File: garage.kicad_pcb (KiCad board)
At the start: 2 copper layers, 9 parts, among them P1 CONN_02X25, P2 CONN_01X02, P3 CONN_02X25, P4 CONN_01X20, P5 CONN_01X20, Q1 ZTX1049a

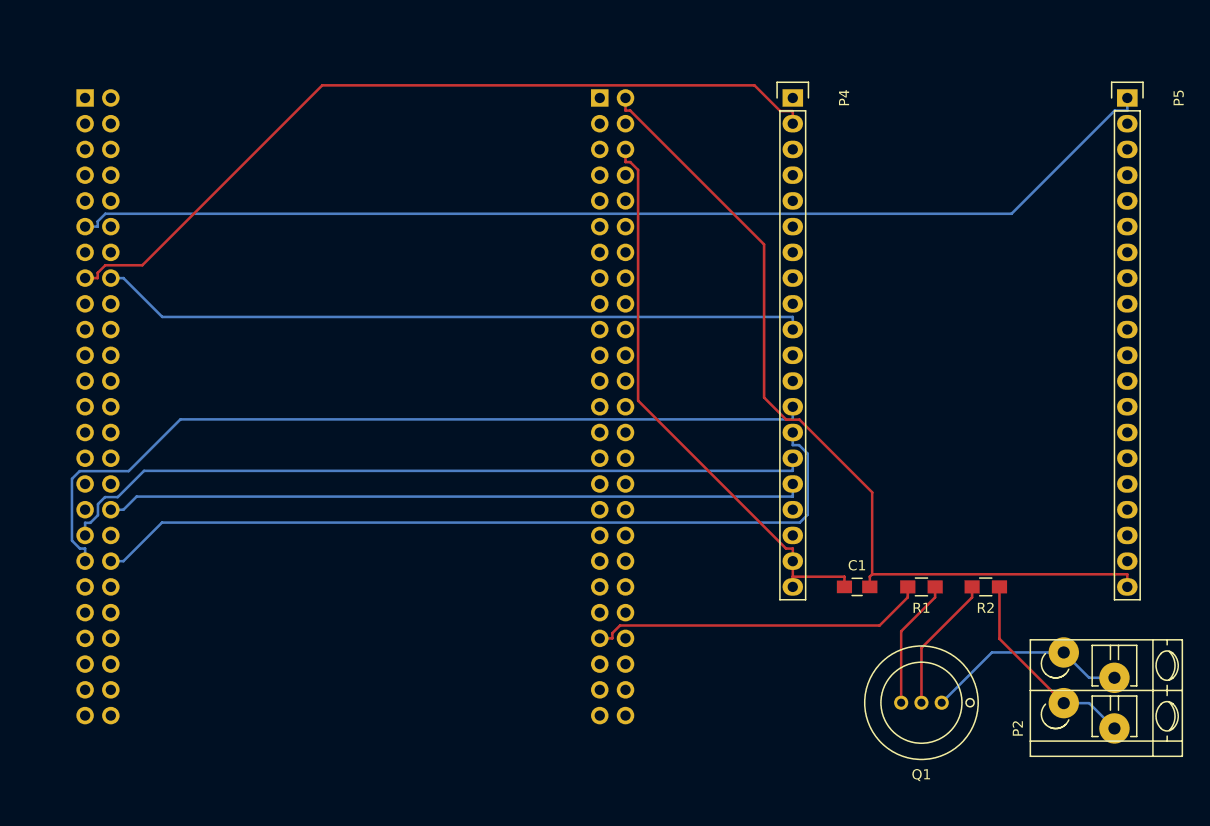
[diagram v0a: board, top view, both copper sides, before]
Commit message: Added board outline
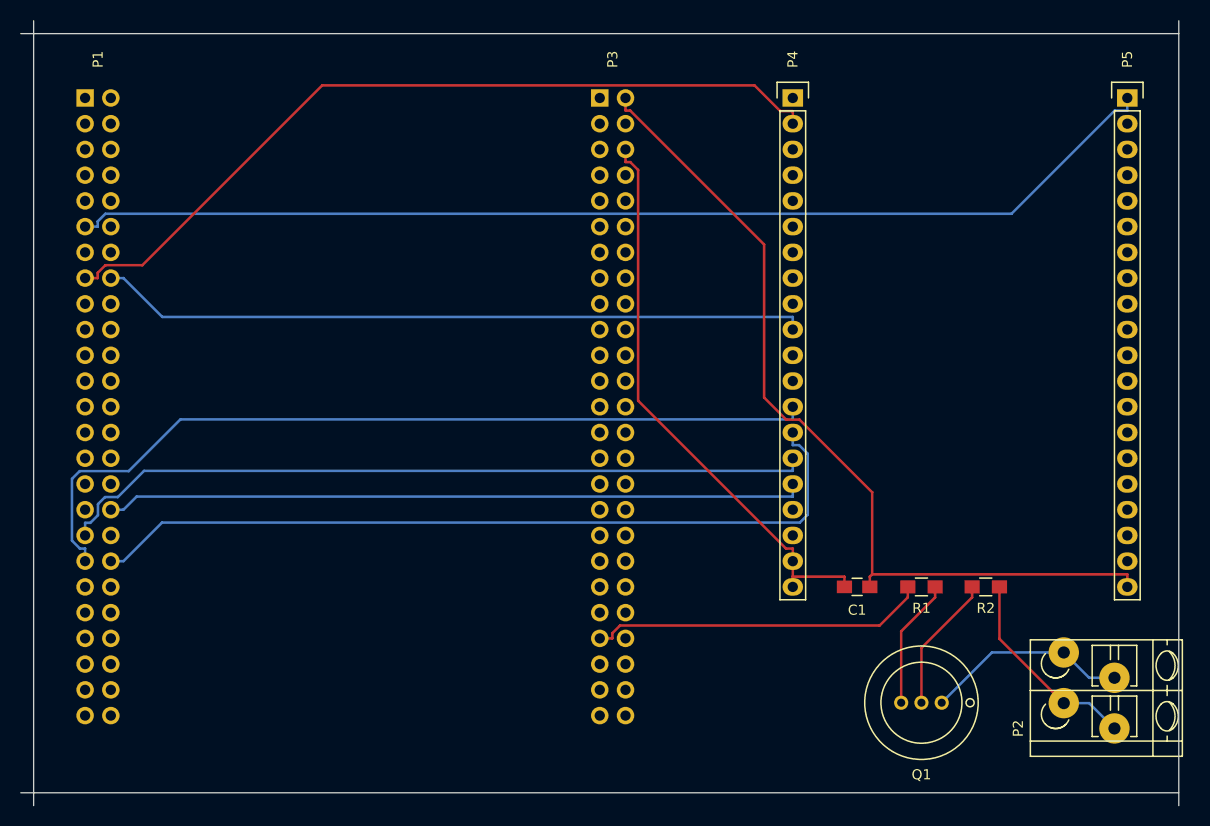
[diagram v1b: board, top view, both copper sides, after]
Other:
- board outline added: 114.3 x 77.5 mm

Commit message: Reduced size of PCB by half
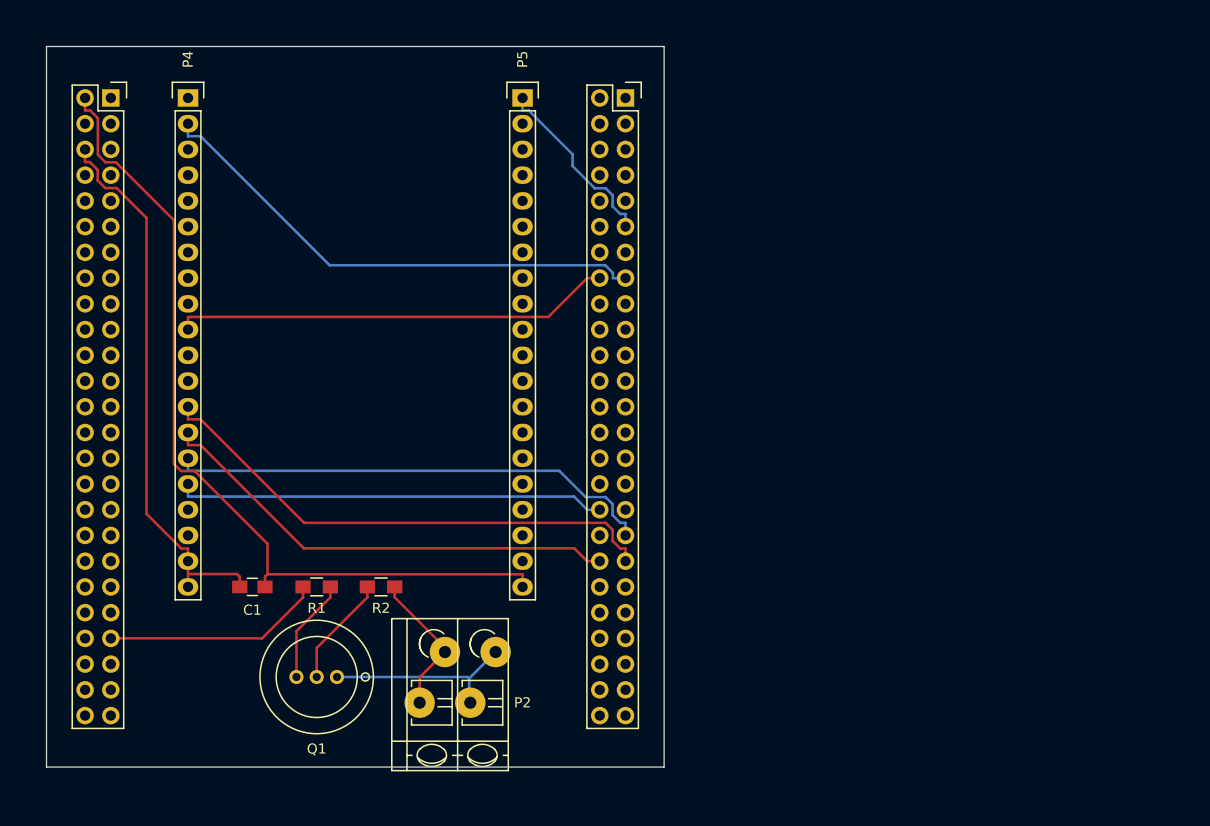
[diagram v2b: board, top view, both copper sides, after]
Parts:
- P1, P3: moved to F.Cu
- moved P2 68.6 mm to (91.4, 96.5), turned to 0 degrees
- moved Q1 59.7 mm to (81.3, 94.0)
- moved P4 59.7 mm to (68.6, 36.8)
- moved C1 59.7 mm to (74.9, 85.1)
- moved P5 59.7 mm to (101.6, 36.8)
- moved R1 59.7 mm to (81.3, 85.1)
- moved R2 59.7 mm to (87.6, 85.1)
- moved P1 53.3 mm to (111.8, 36.8)
- moved P3 48.3 mm to (61.0, 36.8)
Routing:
- net PA1: track 109.2 -> 18.2 mm
- net CTS: track 79.8 -> 46.6 mm
- net RTS: track 83.8 -> 51.6 mm
- net GPIO2: track 80.3 -> 50.5 mm
- net TX: track 75.1 -> 48.4 mm
- net GPIO9: track 70.1 -> 43.5 mm
- net RX: track 69.1 -> 42.4 mm
- net PA8: track 33.4 -> 21.7 mm
- net Garage+: track 20.1 -> 14.5 mm
- net Net-(Q1-Pad3): track 12.8 -> 10.3 mm
- net Net-(Q1-Pad2): track 13.5 -> 11.0 mm
- net GND: track 85.9 -> 83.9 mm
- net 3V: track 56.8 -> 54.9 mm
- net Garage-: track 20.1 -> 19.2 mm
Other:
- board size 114.3 x 77.5 mm -> 61 x 71.1 mm
- rule via_min_drill: 0.508 -> 0.3302
- rule via_min_size: 0.889 -> 0.6858

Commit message: Added ground plane
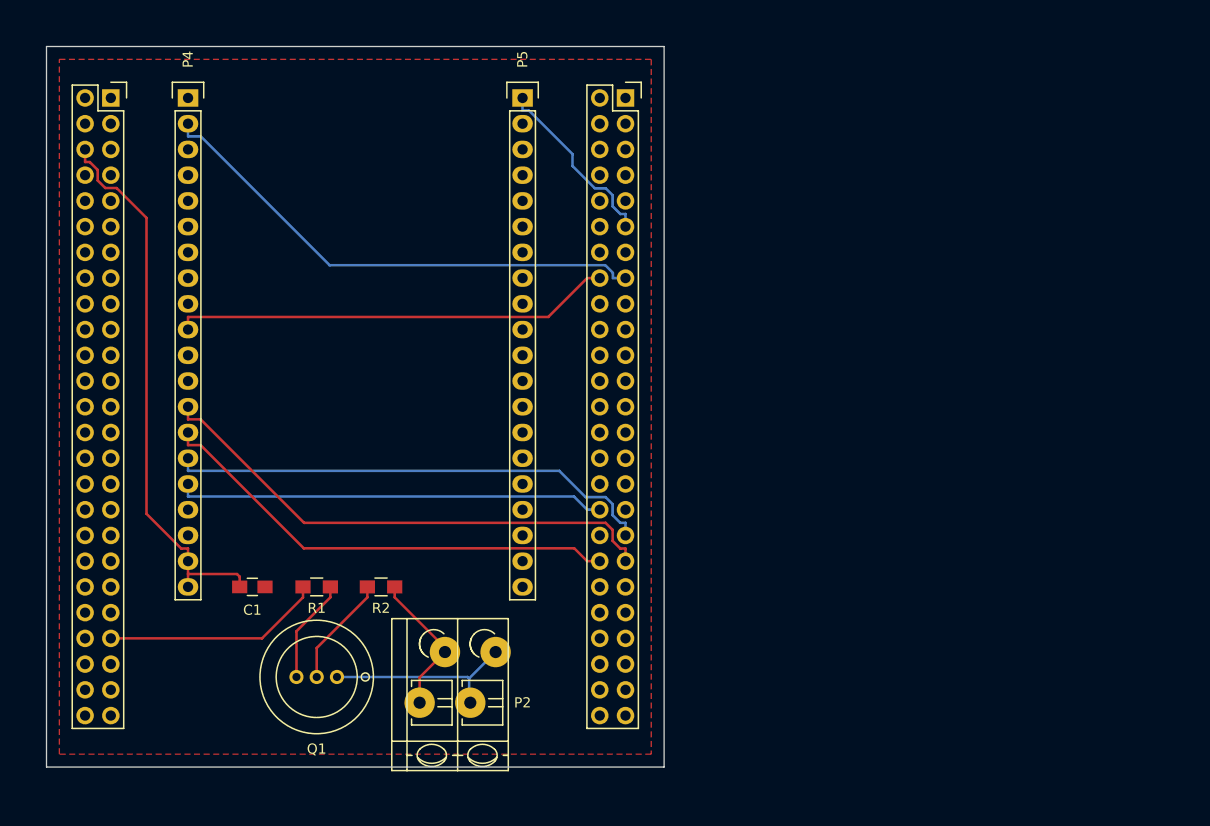
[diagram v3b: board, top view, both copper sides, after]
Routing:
- net GND: track 83.9 -> 0.00 mm
- added copper zone on F.Cu, net GND
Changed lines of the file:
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@@
     (thickness 1.6)
     (drawings 4)
-    (tracks 101)
+    (tracks 85)
     (zones 0)
     (modules 9)
@@
   (segment (start 68.58 83.82) (end 73.4163 83.82) (width 0.254) (layer F.Cu) (net 1))
   (segment (start 73.68 85.09) (end 73.68 84.0837) (width 0.254) (layer F.Cu) (net 1))
-  (segment (start 101.6 85.09) (end 101.6 83.8451) (width 0.254) (layer F.Cu) (net 2))
-  (segment (start 76.18 85.09) (end 76.18 84.0837) (width 0.254) (layer F.Cu) (net 2))
-  (segment (start 58.42 36.83) (end 58.42 38.0749) (width 0.254) (layer F.Cu) (net 2))
-  (segment (start 58.9358 38.0749) (end 58.42 38.0749) (width 0.254) (layer F.Cu) (net 2))
-  (segment (start 59.69 38.8291) (end 58.9358 38.0749) (width 0.254) (layer F.Cu) (net 2))
-  (segment (start 59.69 42.4461) (end 59.69 38.8291) (width 0.254) (layer F.Cu) (net 2))
-  (segment (start 60.4239 43.18) (end 59.69 42.4461) (width 0.254) (layer F.Cu) (net 2))
-  (segment (start 61.4707 43.18) (end 60.4239 43.18) (width 0.254) (layer F.Cu) (net 2))
-  (segment (start 67.1826 48.8919) (end 61.4707 43.18) (width 0.254) (layer F.Cu) (net 2))
-  (segment (start 67.1826 72.9459) (end 67.1826 48.8919) (width 0.254) (layer F.Cu) (net 2))
-  (segment (start 67.8967 73.66) (end 67.1826 72.9459) (width 0.254) (layer F.Cu) (net 2))
-  (segment (start 69.2515 73.66) (end 67.8967 73.66) (width 0.254) (layer F.Cu) (net 2))
-  (segment (start 76.4186 80.8271) (end 69.2515 73.66) (width 0.254) (layer F.Cu) (net 2))
-  (segment (start 76.4186 83.8451) (end 76.4186 80.8271) (width 0.254) (layer F.Cu) (net 2))
-  (segment (start 101.6 83.8451) (end 76.4186 83.8451) (width 0.254) (layer F.Cu) (net 2))
-  (segment (start 76.4186 83.8451) (end 76.18 84.0837) (width 0.254) (layer F.Cu) (net 2))
   (segment (start 111.2442 48.2851) (end 111.76 48.2851) (width 0.254) (layer B.Cu) (net 13))
   (segment (start 110.49 47.5309) (end 111.2442 48.2851) (width 0.254) (layer B.Cu) (net 13))
@@
   (segment (start 82.63 86.1213) (end 79.28 89.4713) (width 0.254) (layer F.Cu) (net 134))
   (segment (start 82.63 85.09) (end 82.63 86.1213) (width 0.254) (layer F.Cu) (net 134))
+  (zone (net 2) (net_name GND) (layer F.Cu) (hatch edge 0.508)
+    (connect_pads (clearance 0.508))
+    (min_thickness 0.254)
+    (fill yes (arc_segments 16) (thermal_gap 0.508) (thermal_bridge_width 0.508))
+    (polygon
+      (pts
+        (xy 114.3 101.6) (xy 55.88 101.6) (xy 55.88 33.02) (xy 114.3 33.02)
+      )
+    )
+  )
 )

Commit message: Updated power and ground planes
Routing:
- net 3V: track 54.9 -> 0.00 mm
- net GND: track 0.00 -> 4.34 mm, vias 0 -> 1
- added copper zone on F.Cu, net 3V
- added copper zone on B.Cu, net GND
- removed copper zone on F.Cu, net GND
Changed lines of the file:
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@@
     (thickness 1.6)
     (drawings 4)
-    (tracks 85)
+    (tracks 72)
     (zones 0)
     (modules 9)
@@
   (gr_line (start 115.57 31.75) (end 115.57 102.87) (angle 90) (layer Edge.Cuts) (width 0.1))
   (gr_line (start 54.61 31.75) (end 115.57 31.75) (angle 90) (layer Edge.Cuts) (width 0.1))
-  (segment (start 58.42 41.91) (end 58.42 43.1549) (width 0.254) (layer F.Cu) (net 1))
-  (segment (start 68.58 82.55) (end 68.58 81.3051) (width 0.254) (layer F.Cu) (net 1))
-  (segment (start 67.9117 81.3051) (end 68.58 81.3051) (width 0.254) (layer F.Cu) (net 1))
-  (segment (start 64.4833 77.8767) (end 67.9117 81.3051) (width 0.254) (layer F.Cu) (net 1))
-  (segment (start 64.4833 48.672) (end 64.4833 77.8767) (width 0.254) (layer F.Cu) (net 1))
-  (segment (start 61.5313 45.72) (end 64.4833 48.672) (width 0.254) (layer F.Cu) (net 1))
-  (segment (start 60.4086 45.72) (end 61.5313 45.72) (width 0.254) (layer F.Cu) (net 1))
-  (segment (start 59.6649 44.9763) (end 60.4086 45.72) (width 0.254) (layer F.Cu) (net 1))
-  (segment (start 59.6649 43.9329) (end 59.6649 44.9763) (width 0.254) (layer F.Cu) (net 1))
-  (segment (start 58.8869 43.1549) (end 59.6649 43.9329) (width 0.254) (layer F.Cu) (net 1))
-  (segment (start 58.42 43.1549) (end 58.8869 43.1549) (width 0.254) (layer F.Cu) (net 1))
-  (segment (start 68.58 85.09) (end 68.58 83.82) (width 0.254) (layer F.Cu) (net 1))
-  (segment (start 68.58 83.82) (end 68.58 82.55) (width 0.254) (layer F.Cu) (net 1))
-  (segment (start 73.4163 83.82) (end 73.68 84.0837) (width 0.254) (layer F.Cu) (net 1))
-  (segment (start 68.58 83.82) (end 73.4163 83.82) (width 0.254) (layer F.Cu) (net 1))
-  (segment (start 73.68 85.09) (end 73.68 84.0837) (width 0.254) (layer F.Cu) (net 1))
+  (segment (start 76.18 85.09) (end 76.18 82.57) (width 0.254) (layer F.Cu) (net 2))
+  (via (at 77.47 81.28) (size 0.889) (layers F.Cu B.Cu) (net 2))
+  (segment (start 76.18 82.57) (end 77.47 81.28) (width 0.254) (layer F.Cu) (net 2))
   (segment (start 111.2442 48.2851) (end 111.76 48.2851) (width 0.254) (layer B.Cu) (net 13))
   (segment (start 110.49 47.5309) (end 111.2442 48.2851) (width 0.254) (layer B.Cu) (net 13))
@@
   (segment (start 82.63 86.1213) (end 79.28 89.4713) (width 0.254) (layer F.Cu) (net 134))
   (segment (start 82.63 85.09) (end 82.63 86.1213) (width 0.254) (layer F.Cu) (net 134))
-  (zone (net 2) (net_name GND) (layer F.Cu) (hatch edge 0.508)
+  (zone (net 1) (net_name 3V) (layer F.Cu) (hatch edge 0.508)
     (connect_pads (clearance 0.508))
     (min_thickness 0.254)
+    (fill yes (arc_segments 16) (thermal_gap 0.508) (thermal_bridge_width 0.508))
+    (polygon
+      (pts
+        (xy 114.3 101.6) (xy 55.88 101.6) (xy 55.88 33.02) (xy 114.3 33.02)
+      )
+    )
+  )
+  (zone (net 2) (net_name GND) (layer B.Cu) (hatch edge 0.508)
+    (connect_pads (clearance 0.508))
+    (min_thickness 0.254)

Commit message: Added silkscreen
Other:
- board text added: "BlueTooth Garage Opener"
- board text added: "Rev A"
- board text added: "SESAME"
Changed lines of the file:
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@@
     (area 56.380999 31.841 120.022334 103.899)
     (thickness 1.6)
-    (drawings 4)
+    (drawings 7)
     (tracks 72)
     (zones 0)
@@
   (page A4)
   (layers
-    (0 F.Cu signal)
-    (31 B.Cu signal)
+    (0 F.Cu signal hide)
+    (31 B.Cu signal hide)
     (32 B.Adhes user)
     (33 F.Adhes user)
@@
     )
   )
+  (gr_text "Rev A" (at 110.49 100.33) (layer B.SilkS)
+    (effects (font (size 0.8 0.8) (thickness 0.12)) (justify mirror))
+  )
+  (gr_text "BlueTooth Garage Opener" (at 69.215 98.425) (layer F.SilkS)
+    (effects (font (size 0.8 0.6) (thickness 0.15) italic))
+  )
+  (gr_text SESAME (at 69.215 96.52) (layer F.SilkS)
+    (effects (font (size 1.5 1.5) (thickness 0.3)))
+  )
   (gr_line (start 54.61 102.87) (end 54.61 31.75) (angle 90) (layer Edge.Cuts) (width 0.1))

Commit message: updated labels
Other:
- rule via_min_size: 0.6858 -> 0.889
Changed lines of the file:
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@@
   (page A4)
   (layers
-    (0 F.Cu signal hide)
-    (31 B.Cu signal hide)
+    (0 F.Cu signal)
+    (31 B.Cu signal)
     (32 B.Adhes user)
     (33 F.Adhes user)
@@
     (via_size 0.889)
     (via_drill 0.635)
-    (via_min_size 0.6858)
+    (via_min_size 0.889)
     (via_min_drill 0.3302)
     (uvia_size 0.508)
@@
     (visible_elements 7FFFFFFF)
     (pcbplotparams
-      (layerselection 0x00030_80000001)
-      (usegerberextensions false)
+      (layerselection 0x010f0_80000001)
+      (usegerberextensions true)
       (excludeedgelayer true)
       (linewidth 0.100000)
@@
       (outputformat 1)
       (mirror false)
-      (drillshape 1)
+      (drillshape 0)
       (scaleselection 1)
-      (outputdirectory ""))
+      (outputdirectory gerber/))
   )
   (net 0 "")

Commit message: Changed traces to match schematic update.
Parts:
- Q1: value ZTX1049a -> 2N3904
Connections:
- P2 pad 2: Garage- -> GND
- Q1 pad 1: Garage- -> GND
- R1 pad 1: Net-(Q1-Pad3) -> Net-(Q1-Pad2)
- R2 pad 2: Net-(Q1-Pad2) -> Net-(Q1-Pad3)
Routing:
- net Garage-: track 19.2 -> 0.00 mm
- net GND: track 4.34 -> 23.6 mm
- net Net-(Q1-Pad3): track 10.3 -> 18.2 mm
- net Net-(Q1-Pad2): track 11.0 -> 9.45 mm
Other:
- board text added: "Rev B"
- board text removed: "Rev A"
